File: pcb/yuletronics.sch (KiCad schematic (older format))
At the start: 35 parts, among them IC1 STM32F042F6P6, IC2 MCP1700, IC3 TLV61225, J1 BATT, J2 MICROUSB, P1 SWD_TC, SW1 BOOTLOAD, SW2 PWR_SWITCH

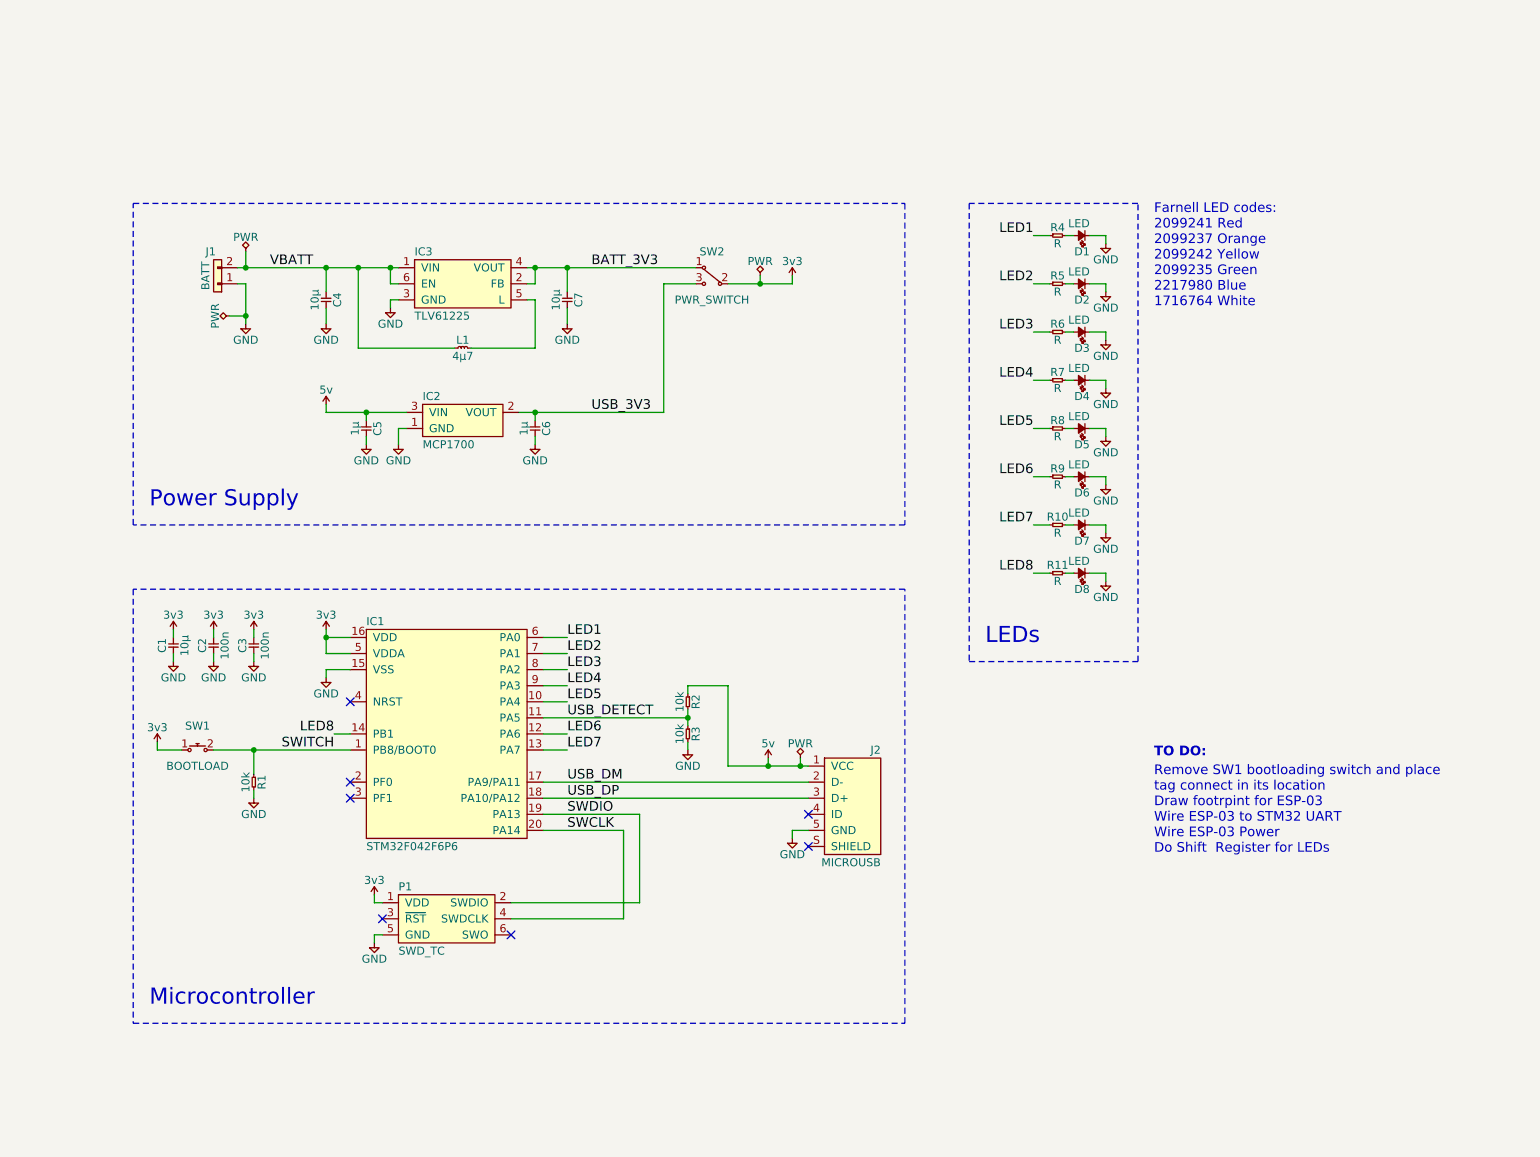
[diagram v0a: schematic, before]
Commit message: Added ESP
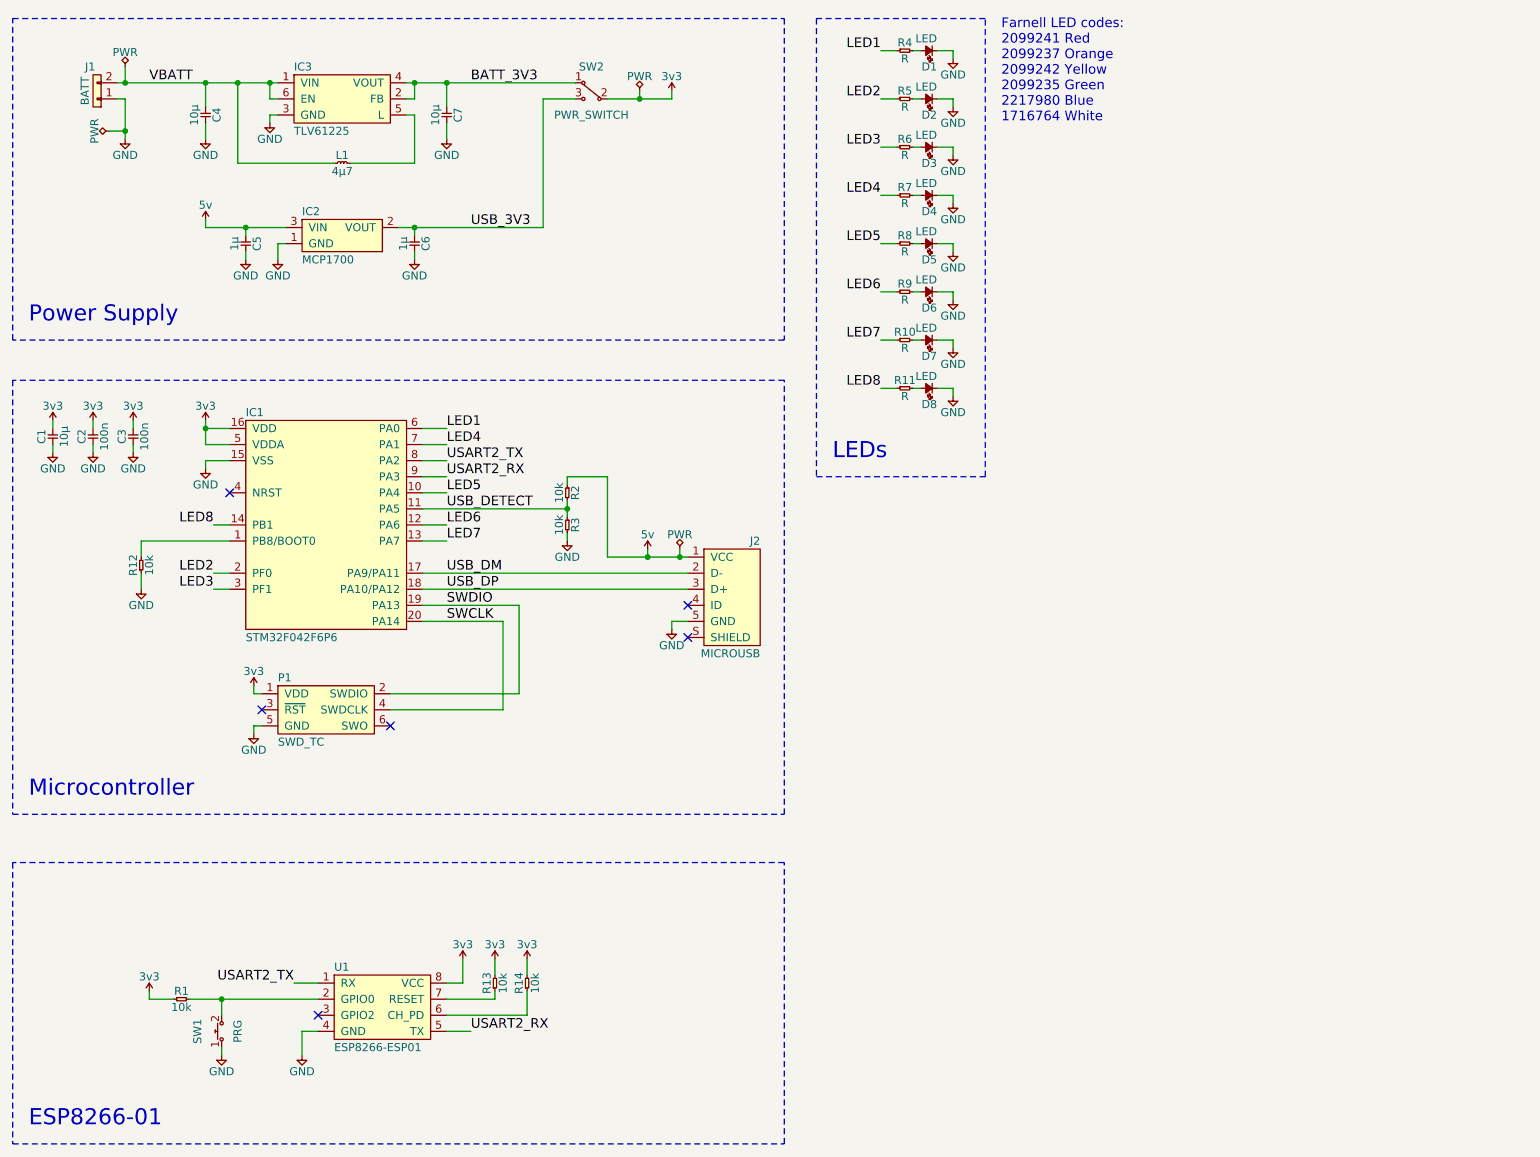
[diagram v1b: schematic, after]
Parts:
- added R12, R13, R14: 10k, agg:0805, symbol R
- added U1: ESP8266-ESP01, agg:ESP8266-ESP01, symbol ESP8266-ESP01
- SW1: value BOOTLOAD -> PRG
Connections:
- net 3v3: now also R1.1, R13.2, R14.2, U1.8 (VCC); no longer SW1.1 ("~")
- net GND: now also SW1.1 ("~"), R12.1, U1.4 (GND); no longer R1.2
- net LED2: now also IC1.2 (PF0); no longer IC1.7 (PA1)
- net LED3: now also IC1.3 (PF1); no longer IC1.8 (PA2)
- net LED4: now also IC1.7 (PA1); no longer IC1.9 (PA3)
- removed net SWITCH: IC1.1 (PB8/BOOT0), R1.1, SW1.2 ("~")
- new net: IC1.1 (PB8/BOOT0), R12.2
- new net: R1.2, SW1.2 ("~"), U1.2 (GPIO0)
- new net: R14.1, U1.6 (CH_PD)
- new net: R13.1, U1.7 (RESET)
- new net USART2_RX: IC1.9 (PA3), U1.5 (TX)
- new net USART2_TX: IC1.8 (PA2), U1.1 (RX)
- no-connect marks 7 -> 6
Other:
- note added: "ESP8266-01"
- note removed: "Remove SW1 bootloading switch and place\ntag connect in its location\nDraw footrpint for ESP-03\nWire ESP-03 to STM32 UART\nWire ESP-03 Power\nDo Shift Register for LEDs"
- note removed: "TO DO:"
- moved on the sheet: C1, C2, C3, C4, C5, C6, C7, D1, D2, D3, D4, D5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

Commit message: Firmware things
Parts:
- R10, R11, R4, R5, R6, R7, R8, R9: value R -> 100R
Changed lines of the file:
@@
 P 6150 850
 F 0 "R4" H 6200 900 50  0000 C CNN
-F 1 "R" H 6200 800 50  0000 C CNN
+F 1 "100R" H 6200 800 50  0000 C CNN
 F 2 "agg:0805" H 6150 850 50  0001 C CNN
 F 3 "" H 6150 850 50  0001 C CNN
@@
 P 6150 1150
 F 0 "R5" H 6200 1200 50  0000 C CNN
-F 1 "R" H 6200 1100 50  0000 C CNN
+F 1 "100R" H 6200 1100 50  0000 C CNN
 F 2 "agg:0805" H 6150 1150 50  0001 C CNN
 F 3 "" H 6150 1150 50  0001 C CNN
@@
 P 6150 1450
 F 0 "R6" H 6200 1500 50  0000 C CNN
-F 1 "R" H 6200 1400 50  0000 C CNN
+F 1 "100R" H 6200 1400 50  0000 C CNN
 F 2 "agg:0805" H 6150 1450 50  0001 C CNN
 F 3 "" H 6150 1450 50  0001 C CNN
@@
 P 6150 1750
 F 0 "R7" H 6200 1800 50  0000 C CNN
-F 1 "R" H 6200 1700 50  0000 C CNN
+F 1 "100R" H 6200 1700 50  0000 C CNN
 F 2 "agg:0805" H 6150 1750 50  0001 C CNN
 F 3 "" H 6150 1750 50  0001 C CNN
@@
 P 6150 2050
 F 0 "R8" H 6200 2100 50  0000 C CNN
-F 1 "R" H 6200 2000 50  0000 C CNN
+F 1 "100R" H 6200 2000 50  0000 C CNN
 F 2 "agg:0805" H 6150 2050 50  0001 C CNN
 F 3 "" H 6150 2050 50  0001 C CNN
@@
 P 6150 2350
 F 0 "R9" H 6200 2400 50  0000 C CNN
-F 1 "R" H 6200 2300 50  0000 C CNN
+F 1 "100R" H 6200 2300 50  0000 C CNN
 F 2 "agg:0805" H 6150 2350 50  0001 C CNN
 F 3 "" H 6150 2350 50  0001 C CNN
@@
 P 6150 2650
 F 0 "R10" H 6200 2700 50  0000 C CNN
-F 1 "R" H 6200 2600 50  0000 C CNN
+F 1 "100R" H 6200 2600 50  0000 C CNN
 F 2 "agg:0805" H 6150 2650 50  0001 C CNN
 F 3 "" H 6150 2650 50  0001 C CNN
@@
 P 6150 2950
 F 0 "R11" H 6200 3000 50  0000 C CNN
-F 1 "R" H 6200 2900 50  0000 C CNN
+F 1 "100R" H 6200 2900 50  0000 C CNN
 F 2 "agg:0805" H 6150 2950 50  0001 C CNN
 F 3 "" H 6150 2950 50  0001 C CNN
